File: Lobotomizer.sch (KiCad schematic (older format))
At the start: 3 parts, among them J1 IN, J2 OUT, J3 Barrel_Jack

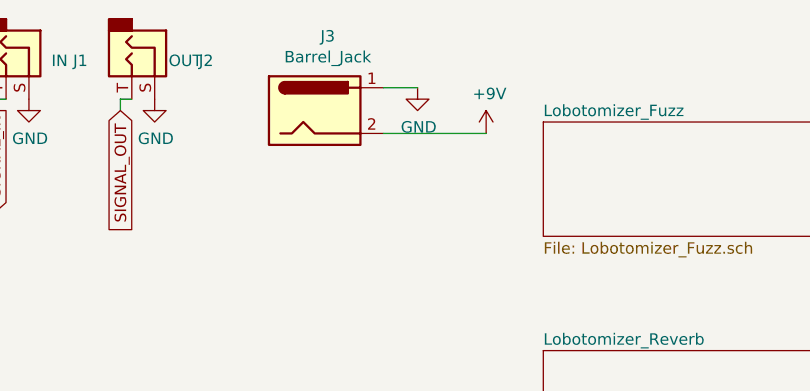
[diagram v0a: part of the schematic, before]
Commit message: fixed major error
U207:7 now connected to VCLEAN.
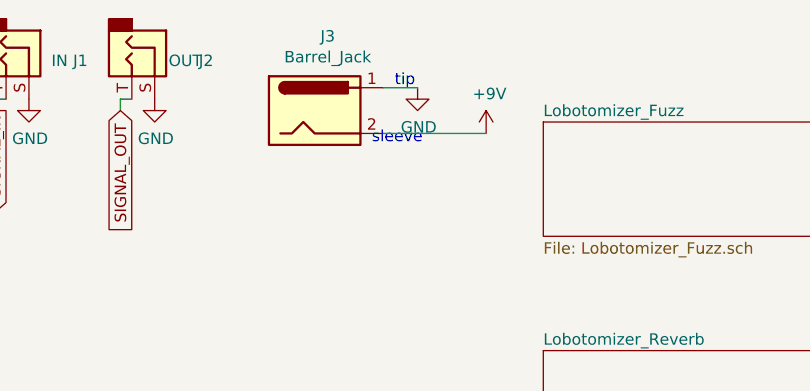
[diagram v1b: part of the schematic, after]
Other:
- note added: "sleeve\n"
- note added: "tip\n"
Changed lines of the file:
@@
 Wire Wire Line
 	2300 850  2450 850
+Text Notes 2250 1100 0    50   ~ 0
+sleeve\n
+Text Notes 2350 850  0    50   ~ 0
+tip\n
 $EndSCHEMATC

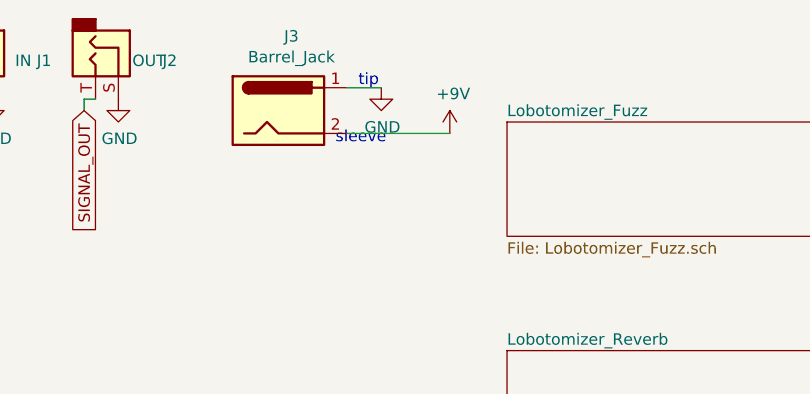
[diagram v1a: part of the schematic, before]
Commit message: changed to pos tip, gnd sleeve jack.
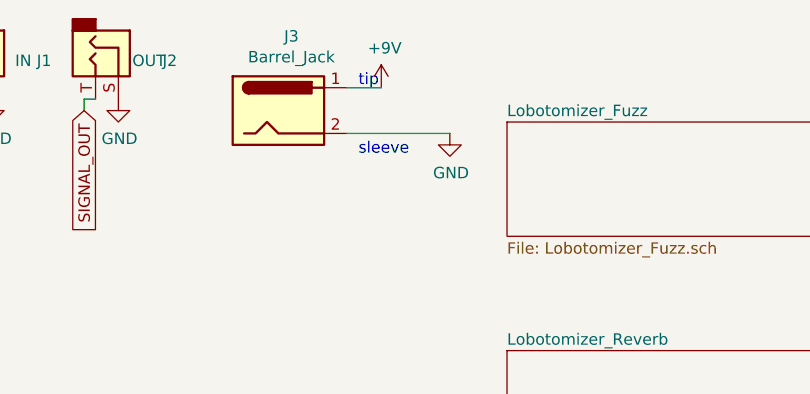
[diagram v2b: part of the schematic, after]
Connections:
- net +9V: now also J3.1; no longer J3.2
- net GND: now also J3.2; no longer J3.1
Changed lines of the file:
@@
 L power:GND #PWR0112
 U 1 1 61CA2545
-P 2450 850
-F 0 "#PWR0112" H 2450 600 50  0001 C CNN
-F 1 "GND" H 2455 677 50  0000 C CNN
-F 2 "" H 2450 850 50  0001 C CNN
-F 3 "" H 2450 850 50  0001 C CNN
-	1    2450 850
+P 2750 1050
+F 0 "#PWR0112" H 2750 800 50  0001 C CNN
+F 1 "GND" H 2755 877 50  0000 C CNN
+F 2 "" H 2750 1050 50  0001 C CNN
+F 3 "" H 2750 1050 50  0001 C CNN
+	1    2750 1050
 	1    0    0    -1
 $EndComp
@@
 L power:+9V #PWR0113
 U 1 1 61CA29CB
-P 2750 1050
-F 0 "#PWR0113" H 2750 900 50  0001 C CNN
-F 1 "+9V" H 2765 1223 50  0000 C CNN
-F 2 "" H 2750 1050 50  0001 C CNN
-F 3 "" H 2750 1050 50  0001 C CNN
-	1    2750 1050
+P 2450 850
+F 0 "#PWR0113" H 2450 700 50  0001 C CNN
+F 1 "+9V" H 2465 1023 50  0000 C CNN
+F 2 "" H 2450 850 50  0001 C CNN
+F 3 "" H 2450 850 50  0001 C CNN
+	1    2450 850
 	1    0    0    -1
 $EndComp
@@
 Wire Wire Line
 	2300 850  2450 850
-Text Notes 2250 1100 0    50   ~ 0
+Text Notes 2350 1150 0    50   ~ 0
 sleeve\n
 Text Notes 2350 850  0    50   ~ 0

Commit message: lobotomizer v2 update
so much changed i cant note it all here
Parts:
- added C1: 1n, Capacitor_THT:C_Disc_D3.8mm_W2.6mm_P2.50mm, symbol Device:C
- added C2: 680p, Capacitor_THT:C_Disc_D4.3mm_W1.9mm_P5.00mm, symbol Device:C
- added R1, R2, R3, R4, R5, R6, R7, R8, R9: 100K, Resistor_THT:R_Axial_DIN0204_L3.6mm_D1.6mm_P5.08mm_Horizontal, symbol Device:R
- added RV1, RV2, RV3, RV4: 100K, Potentiometer_THT:Potentiometer_Bourns_3266Y_Vertical, symbol Device:R_POT
- added SW1, SW2, SW3, SW4: SW_SPDT, TerminalBlock_Phoenix:TerminalBlock_Phoenix_MKDS-1,5-3-5.08_1x03_P5.08mm_Horizontal, symbol Switch:SW_SPDT
- added U1: TL082, Package_DIP:DIP-8_W7.62mm, symbol Device:Opamp_Dual_Generic
- J1, J2: footprint Connector_Audio:Jack_6.35mm_Neutrik_NMJ4HCD2_Horizontal -> Connector_Audio:Jack_6.35mm_Neutrik_NMJ4HFD2_Horizontal
- J3: value Barrel_Jack -> POWER; footprint Connector_BarrelJack:BarrelJack_Horizontal -> Connector_BarrelJack:BarrelJack_CUI_PJ-063AH_Horizontal
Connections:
- net GND: now also C1.2, C2.2, RV1.3, RV2.3, RV3.3, RV4.3, U1.3 (+), U1.4 (V-), U1.5 (+)
- net SIGNAL_IN: now also SW1.3 (C)
- net SIGNAL_OUT: no longer names the net of J2.T
- net SIGNAL_OUT: now also C2.1, R9.1
- new net: RV3.1, SW3.2 (B)
- new net: RV2.1, SW2.2 (B)
- new net: RV1.1, SW1.2 (B)
- new net: RV4.1, SW4.2 (B)
- new net: R1.2, RV1.2
- new net: R2.2, RV2.2
- new net: R3.2, RV3.2
- new net: R4.2, RV4.2
- new net: R1.1, R2.1, R3.1, R4.1, R5.2, U1.2 (-)
- new net: R5.1, R6.2, U1.1
- new net: R6.1, R7.2, U1.6 (-)
- new net: R7.1, R8.2, U1.7
- new net: C1.1, R8.1, R9.2
- new net FUZZ_OUT: SW2.3 (C)
- new net MEGAFUCKER_OUT: SW3.3 (C)
- new net SAW_OUT: SW4.3 (C)
- new net VCLEAN: U1.8 (V+)
- no-connect marks 0 -> 4
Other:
- moved on the sheet: J2, J3
